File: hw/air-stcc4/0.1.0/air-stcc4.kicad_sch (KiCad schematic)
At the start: 12 parts, among them J1 BM04B-SRSS-TB(LF)(SN), J2 BM04B-SRSS-TB(LF)(SN), J3 Conn_01x05, U1 STCC4, U2 SHT40

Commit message: added CTRLH logo ; fixed MPN for 10K resistors
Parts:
- R3, R4: LCSC C23162 -> C25804
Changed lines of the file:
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@@
 			)
 		)
-		(property "LCSC" "C23162"
+		(property "LCSC" "C25804"
 			(at 35.56 102.87 0)
 			(effects
@@
 			)
 		)
-		(property "LCSC" "C23162"
+		(property "LCSC" "C25804"
 			(at 16.51 102.87 0)
 			(effects

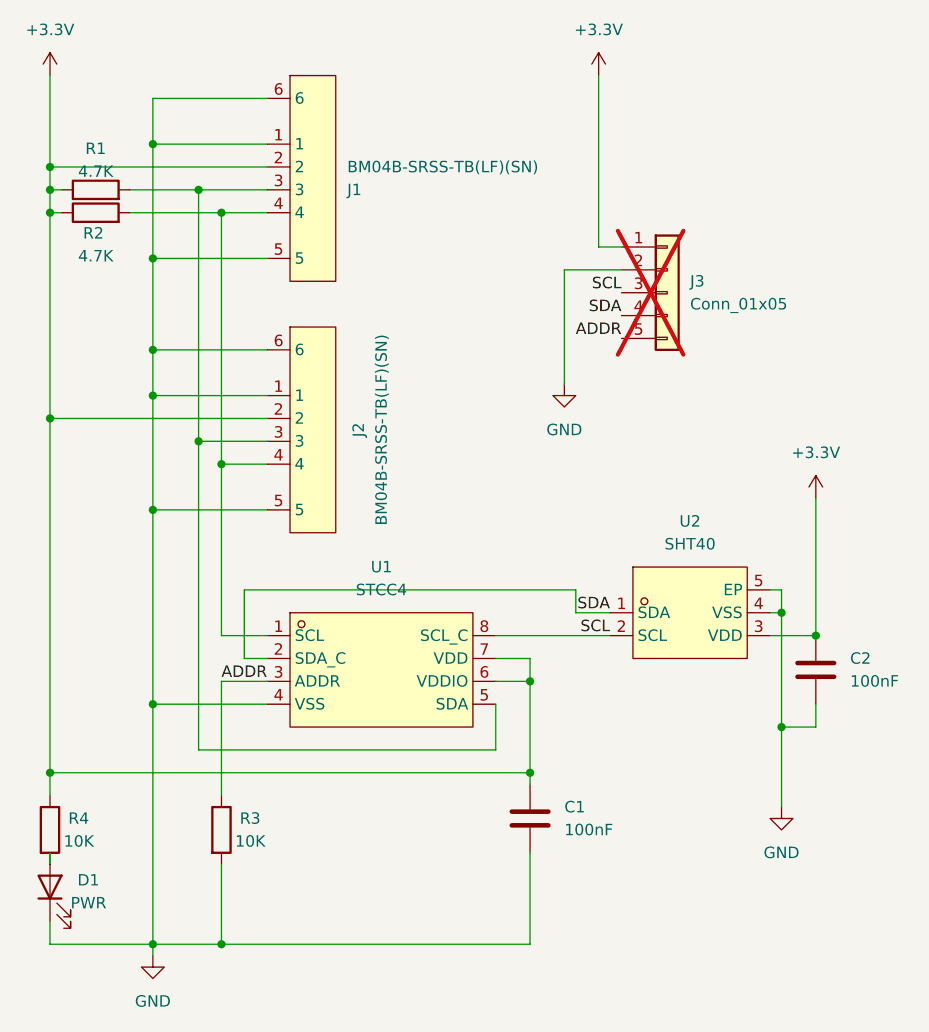
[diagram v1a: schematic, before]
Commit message: doc improvements
fixed LED footprint on air-stcc4/0.1.0 (changed to 0603)
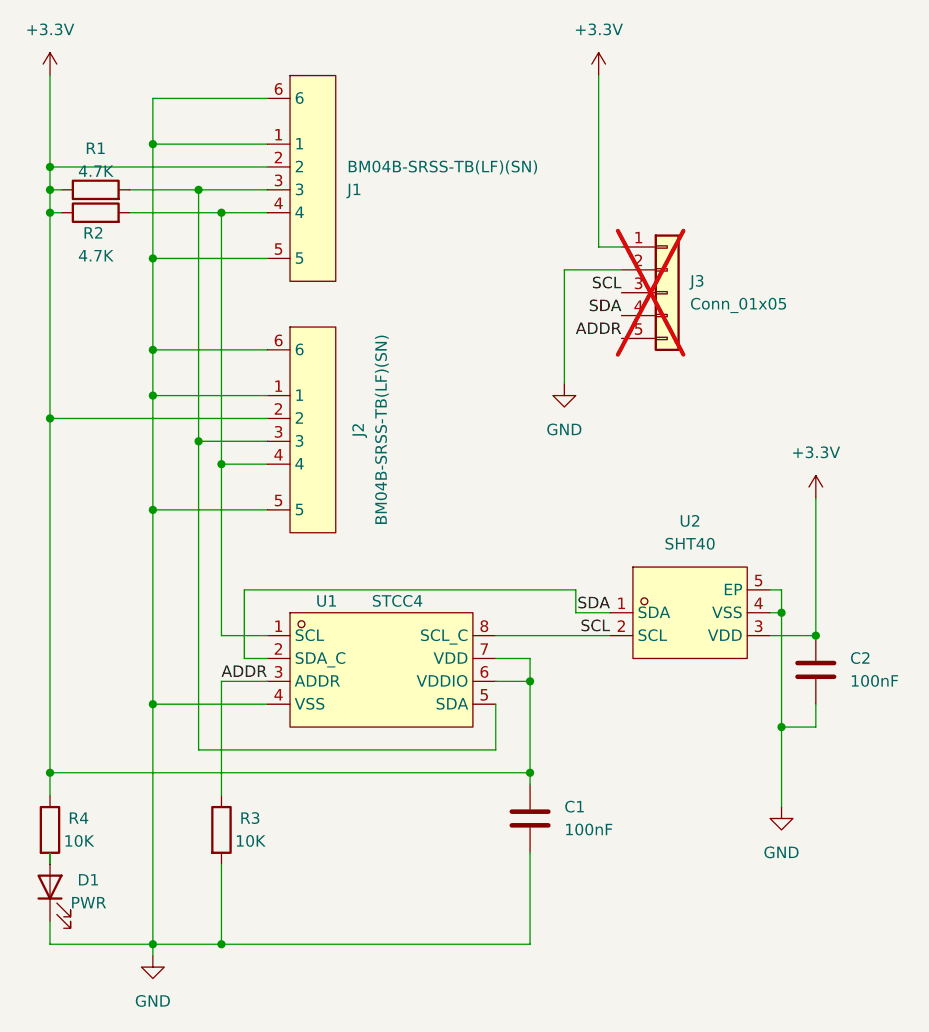
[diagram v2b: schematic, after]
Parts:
- D1: footprint LED_SMD:LED_0201_0603Metric_Pad0.64x0.40mm_HandSolder -> LED_SMD:LED_0603_1608Metric_Pad1.05x0.95mm_HandSolder
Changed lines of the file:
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@@
 		(company "PDX Hackerspace")
 		(comment 1 "John Romkey")
+		(comment 2 "License: CERN-OHL-S License: CERN-OHL-S https://ohwr.org/cern_ohl_s_v2.pdf")
 	)
 	(junction
@@
 			)
 		)
-		(property "Footprint" "LED_SMD:LED_0201_0603Metric_Pad0.64x0.40mm_HandSolder"
+		(property "Footprint" "LED_SMD:LED_0603_1608Metric_Pad1.05x0.95mm_HandSolder"
 			(at 16.51 109.22 0)
 			(effects
@@
 		(on_board yes)
 		(dnp no)
-		(fields_autoplaced yes)
 		(property "Reference" "U1"
-			(at 53.34 73.66 0)
+			(at 47.244 77.47 0)
 			(effects
 				(font
@@
 		)
 		(property "Value" "STCC4"
-			(at 53.34 76.2 0)
-			(effects
-				(font
+			(at 55.118 77.47 0)
+			(effects
+				(font
